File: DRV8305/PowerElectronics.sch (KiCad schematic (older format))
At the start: 41 parts, among them J13 MotorVSense, J14 Motor, J15 PWR_Out, J8 MotorPower, Q1 U_High, Q2 U_Low, Q3 U_High, Q4 U_Low, Q5 U_High, Q6 U_Low, U3 CSRV065V0P, U4 AP111733

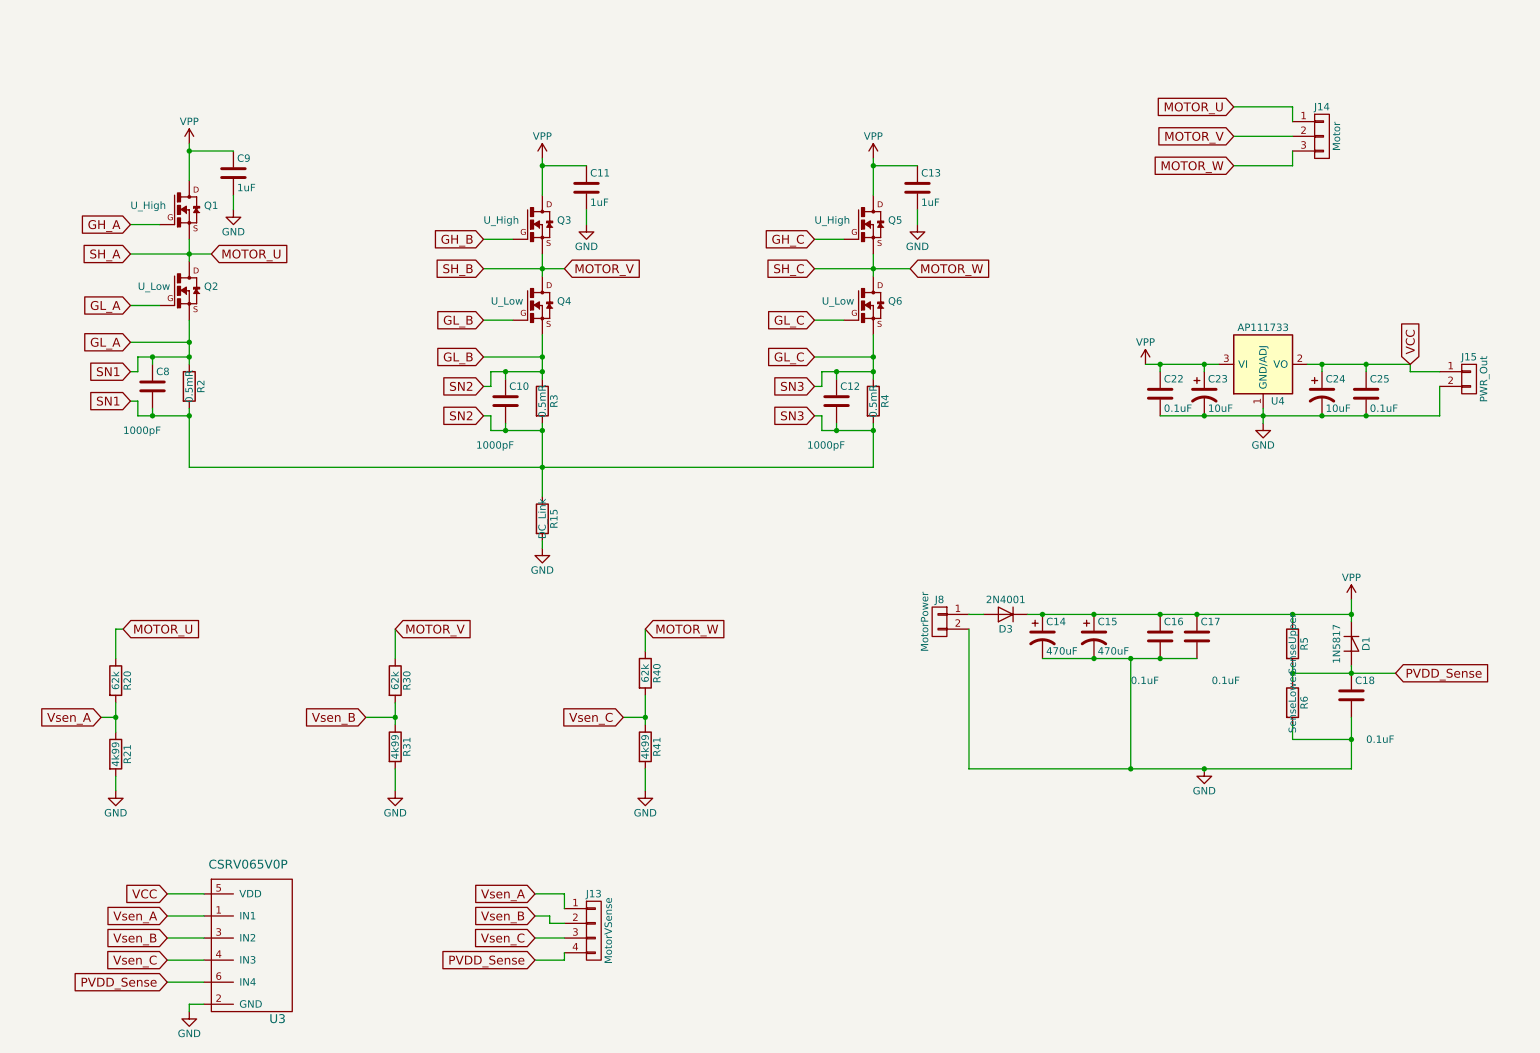
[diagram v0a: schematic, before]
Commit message: Seperated out BLDC
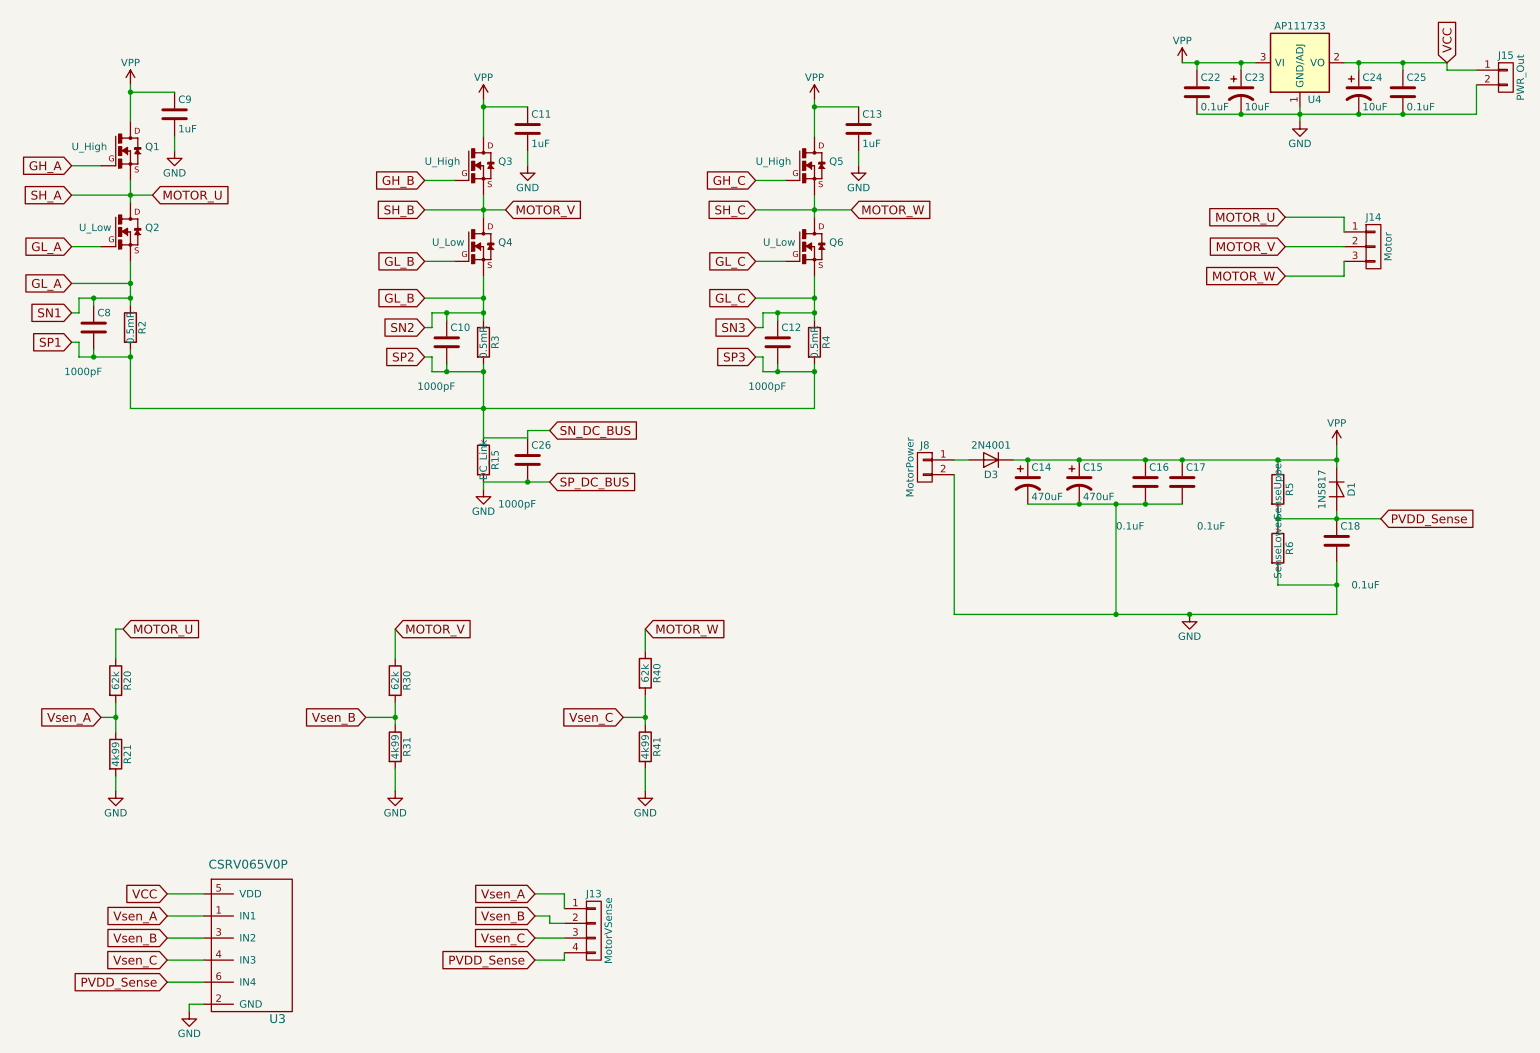
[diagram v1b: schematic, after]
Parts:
- added C26: 1000pF, Capacitors_SMD:C_1206_HandSoldering, symbol C
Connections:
- net GL_A: no longer C10.1, C10.2, C12.1, C12.2, C8.2, Q4.1 (S), Q4.2 (S), Q4.3 (S), Q4.4 (G), Q6.1 (S), Q6.2 (S), Q6.3 (S), Q6.4 (G), R15.1, R2.2, R3.1, R3.2, R4.1, R4.2
- net GND: now also C26.2
- new net GL_B: C10.1, Q4.1 (S), Q4.2 (S), Q4.3 (S), Q4.4 (G), R3.1
- new net GL_C: C12.1, Q6.1 (S), Q6.2 (S), Q6.3 (S), Q6.4 (G), R4.1
- new net SN_DC_BUS: C10.2, C12.2, C26.1, C8.2, R15.1, R2.2, R3.2, R4.2
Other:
- moved on the sheet: C10, C11, C12, C13, C14, C15, C16, C17, C18, C22, C23, C24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
